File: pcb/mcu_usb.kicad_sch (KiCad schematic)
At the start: 31 parts, among them J12 USB_C_Receptacle, J13 UPDI, U10 CP2102N-A02-GQFN24, U11 LP2985-3.3, U9 AVR128DA32-I/PT, Y1 32.768kHz

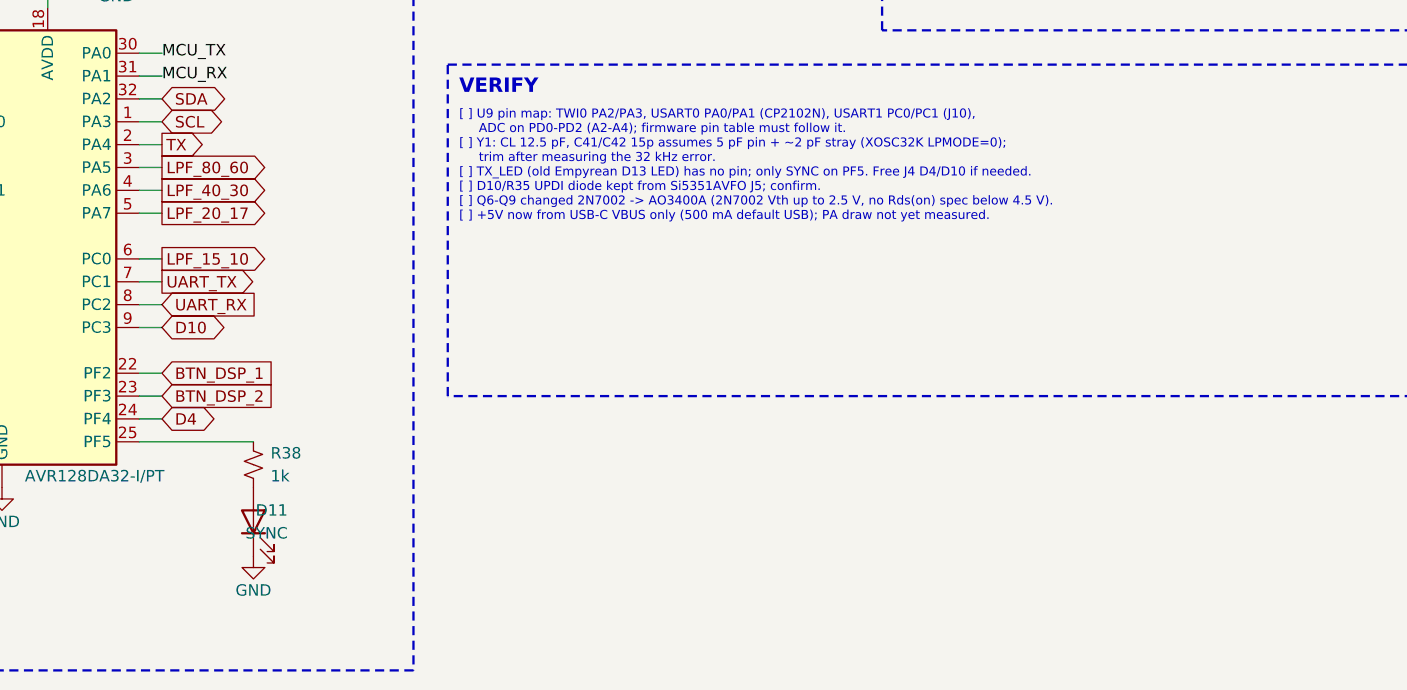
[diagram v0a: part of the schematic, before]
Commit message: Add TX LED on TX keying net; fix USART1 pin assignment
- D12 KT-0603YG (C2289) + R39 470R (C23179) from TX (PA4) to GND, ~2.6 mA
- PC0/PC1 now UART_TX/UART_RX (USART1 default pins), LPF_15_10 moved to PC2
- ERC 0 errors; PDF regenerated; VERIFY.md TX_LED item resolved
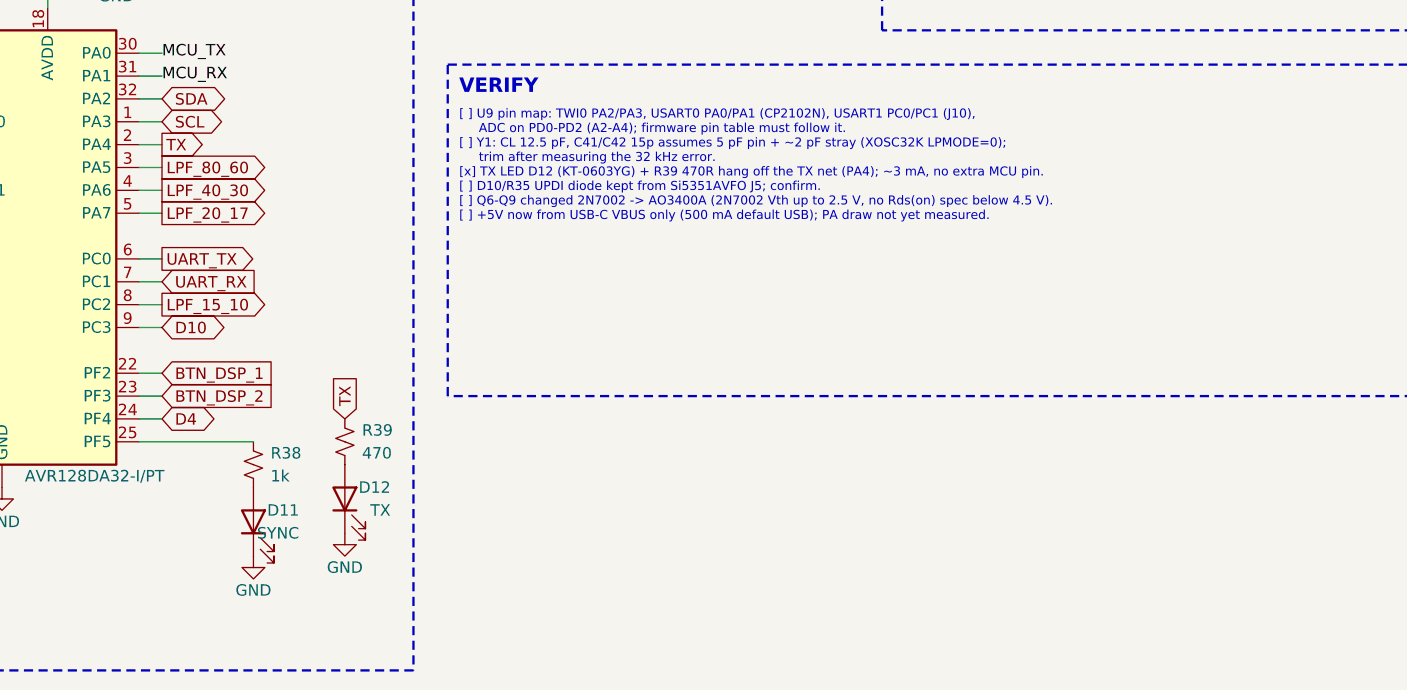
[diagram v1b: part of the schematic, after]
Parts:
- added D12: TX, LED_SMD:LED_0603_1608Metric, symbol Device:LED
- added R39: 470, Resistor_SMD:R_0603_1608Metric, symbol Device:R_Small_US
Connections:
- net GND: now also D12.1 (K)
- net LPF_15_10: now also U9.8 (PC2); no longer U9.6 (PC0)
- net TX: now also R39.1
- net UART_RX: now also U9.7 (PC1); no longer U9.8 (PC2)
- net UART_TX: now also U9.6 (PC0); no longer U9.7 (PC1)
- new net: D12.2 (A), R39.2
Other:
- note added: "[ ] U9 pin map: TWI0 PA2/PA3, USART0 PA0/PA1 (CP2102N), USART1 PC0/PC1 (J10), ADC on PD0-PD2 (A2-A4); firmware pin table must follow it. [ ] Y1: CL 12.5 pF, C41/C42 15p assumes 5 pF pin + ~2 pF stray (XOSC32K LPMODE=0); trim after measuring the 32 kHz error. [x] TX LED D12 (KT-0603YG) + R39 470R hang off the TX net (PA4); ~3 mA, no extra MCU pin. [ ] D10/R35 UPDI diode kept from Si5351AVFO J5; co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"
- note removed: "[ ] U9 pin map: TWI0 PA2/PA3, USART0 PA0/PA1 (CP2102N), USART1 PC0/PC1 (J10), ADC on PD0-PD2 (A2-A4); firmware pin table must follow it. [ ] Y1: CL 12.5 pF, C41/C42 15p assumes 5 pF pin + ~2 pF stray (XOSC32K LPMODE=0); trim after measuring the 32 kHz error. [ ] TX_LED (old Empyrean D13 LED) has no pin; only SYNC on PF5. Free J4 D4/D10 if needed. [ ] D10/R35 UPDI diode kept from Si5351AVFO J5; co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"

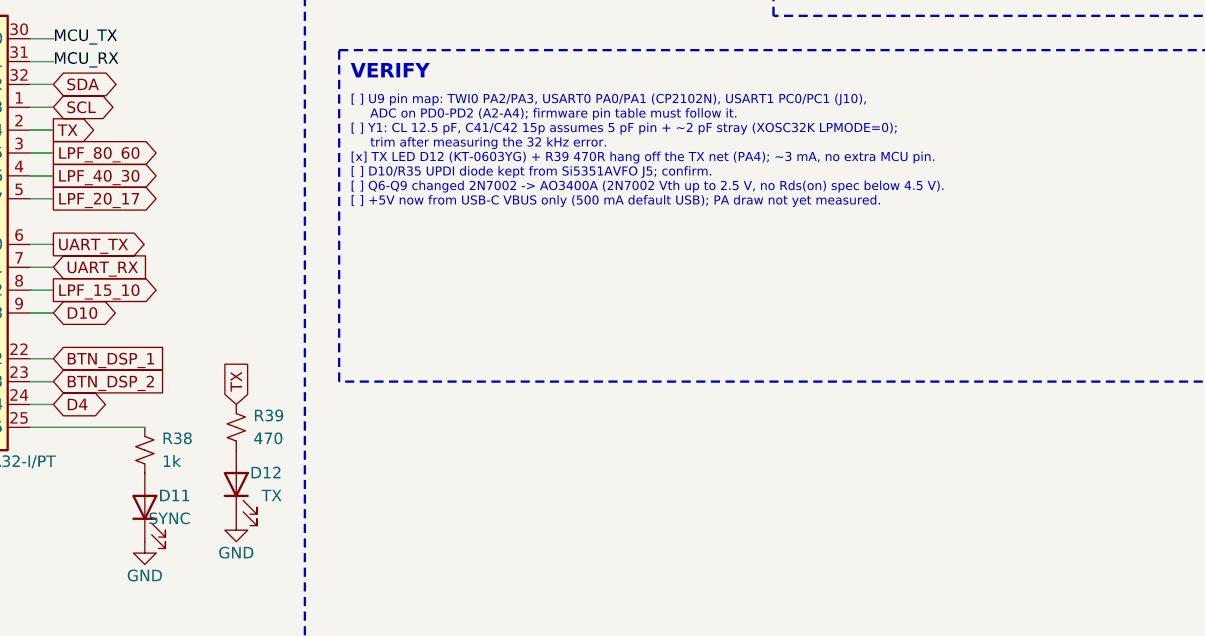
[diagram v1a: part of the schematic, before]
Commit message: Sync LED to yellow KT-0603Y with 470R; confirm UPDI matches Si5351AVFO/EtherKeyerMini
- D11 KT-0603Y (C2287), R38 470R (C23179), ~2-3 mA
- VERIFY.md: UPDI and sync LED items resolved; U1 FB stays open
- ERC 0 errors; PDF regenerated
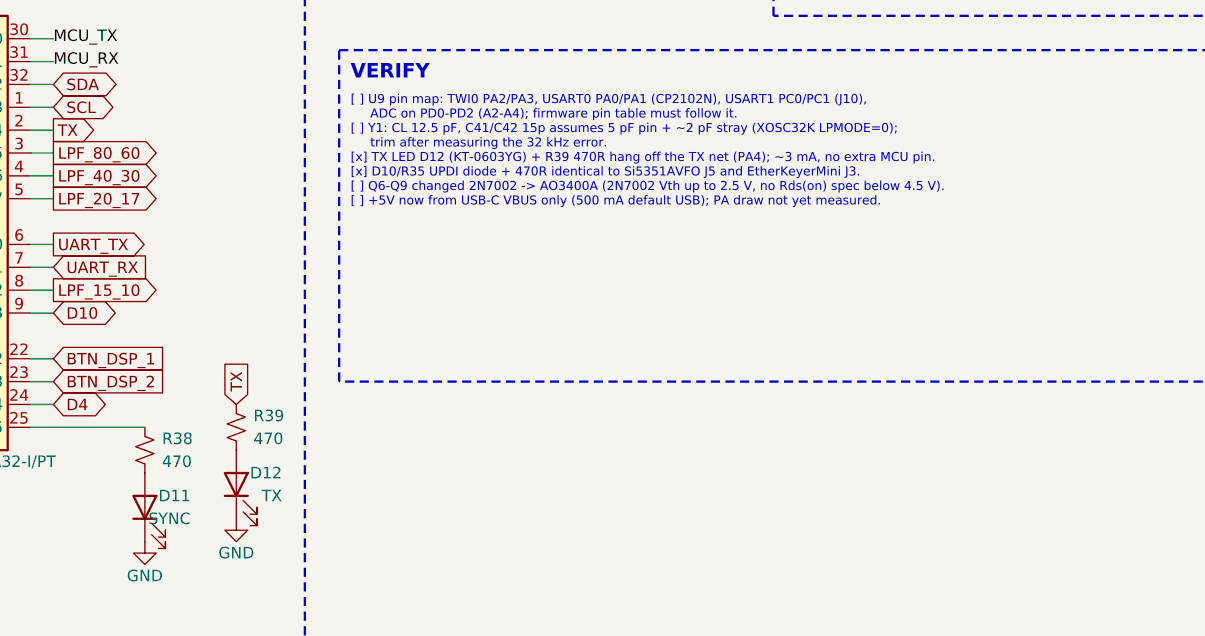
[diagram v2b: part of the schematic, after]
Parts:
- D11: LCSC C2286 -> C2287; MPN KT-0603R -> KT-0603Y
- R38: value 1k -> 470; LCSC C21190 -> C23179; MPN 0603WAF1001T5E -> 0603WAF4700T5E
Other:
- note added: "[ ] U9 pin map: TWI0 PA2/PA3, USART0 PA0/PA1 (CP2102N), USART1 PC0/PC1 (J10), ADC on PD0-PD2 (A2-A4); firmware pin table must follow it. [ ] Y1: CL 12.5 pF, C41/C42 15p assumes 5 pF pin + ~2 pF stray (XOSC32K LPMODE=0); trim after measuring the 32 kHz error. [x] TX LED D12 (KT-0603YG) + R39 470R hang off the TX net (PA4); ~3 mA, no extra MCU pin. [x] D10/R35 UPDI diode + 470R identical to Si5351A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"
- note removed: "[ ] U9 pin map: TWI0 PA2/PA3, USART0 PA0/PA1 (CP2102N), USART1 PC0/PC1 (J10), ADC on PD0-PD2 (A2-A4); firmware pin table must follow it. [ ] Y1: CL 12.5 pF, C41/C42 15p assumes 5 pF pin + ~2 pF stray (XOSC32K LPMODE=0); trim after measuring the 32 kHz error. [x] TX LED D12 (KT-0603YG) + R39 470R hang off the TX net (PA4); ~3 mA, no extra MCU pin. [ ] D10/R35 UPDI diode kept from Si5351AVFO J5; co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"
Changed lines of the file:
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@@
 			)
 		)
-		(property "Value" "1k"
+		(property "Value" "470"
 			(at 131.445 173.99 0)
 			(effects
@@
 			)
 		)
-		(property "MPN" "0603WAF1001T5E"
+		(property "MPN" "0603WAF4700T5E"
 			(at 129.54 172.72 0)
 			(effects
@@
 			)
 		)
-		(property "LCSC" "C21190"
+		(property "LCSC" "C23179"
 			(at 129.54 172.72 0)
 			(effects
@@
 			)
 		)
-		(property "MPN" "KT-0603R"
+		(property "MPN" "KT-0603Y"
 			(at 129.54 179.07 0)
 			(effects
@@
 			)
 		)
-		(property "LCSC" "C2286"
+		(property "LCSC" "C2287"
 			(at 129.54 179.07 0)
 			(effects
@@
 		)
 	)
-	(text "[ ] U9 pin map: TWI0 PA2/PA3, USART0 PA0/PA1 (CP2102N), USART1 PC0/PC1 (J10),\n     ADC on PD0-PD2 (A2-A4); firmware pin table must follow it.\n[ ] Y1: CL 12.5 pF, C41/C42 15p assumes 5 pF pin + ~2 pF stray (XOSC32K LPMODE=0);\n     trim after measuring the 32 kHz error.\n[x] TX LED D12 (KT-0603YG) + R39 470R hang off the TX net (PA4); ~3 mA, no extra MCU pin.\n[ ] D10/R35 UPDI diode kept from Si5351AVFO J5; confirm.\n[ ] Q6-Q9 changed 2N7002 -> AO3400A (2N7002 Vth up to 2.5 V, no Rds(on) spec below 4.5 V).\n[ ] +5V now from USB-C VBUS only (500 mA default USB); PA draw not yet measured."
+	(text "[ ] U9 pin map: TWI0 PA2/PA3, USART0 PA0/PA1 (CP2102N), USART1 PC0/PC1 (J10),\n     ADC on PD0-PD2 (A2-A4); firmware pin table must follow it.\n[ ] Y1: CL 12.5 pF, C41/C42 15p assumes 5 pF pin + ~2 pF stray (XOSC32K LPMODE=0);\n     trim after measuring the 32 kHz error.\n[x] TX LED D12 (KT-0603YG) + R39 470R hang off the TX net (PA4); ~3 mA, no extra MCU pin.\n[x] D10/R35 UPDI diode + 470R identical to Si5351AVFO J5 and EtherKeyerMini J3.\n[ ] Q6-Q9 changed 2N7002 -> AO3400A (2N7002 Vth up to 2.5 V, no Rds(on) spec below 4.5 V).\n[ ] +5V now from USB-C VBUS only (500 mA default USB); PA draw not yet measured."
 		(exclude_from_sim no)
 		(at 152.4 133.35 0)

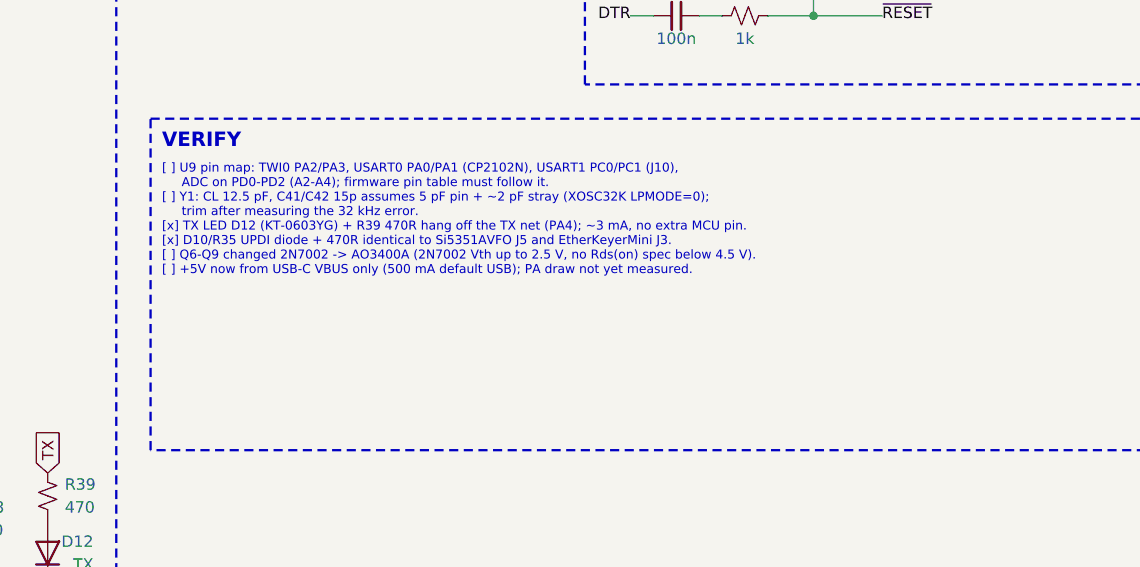
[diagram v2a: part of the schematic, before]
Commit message: VERIFY: resolve U1 FB item (FB tied to VIN selects internal 12 V output)
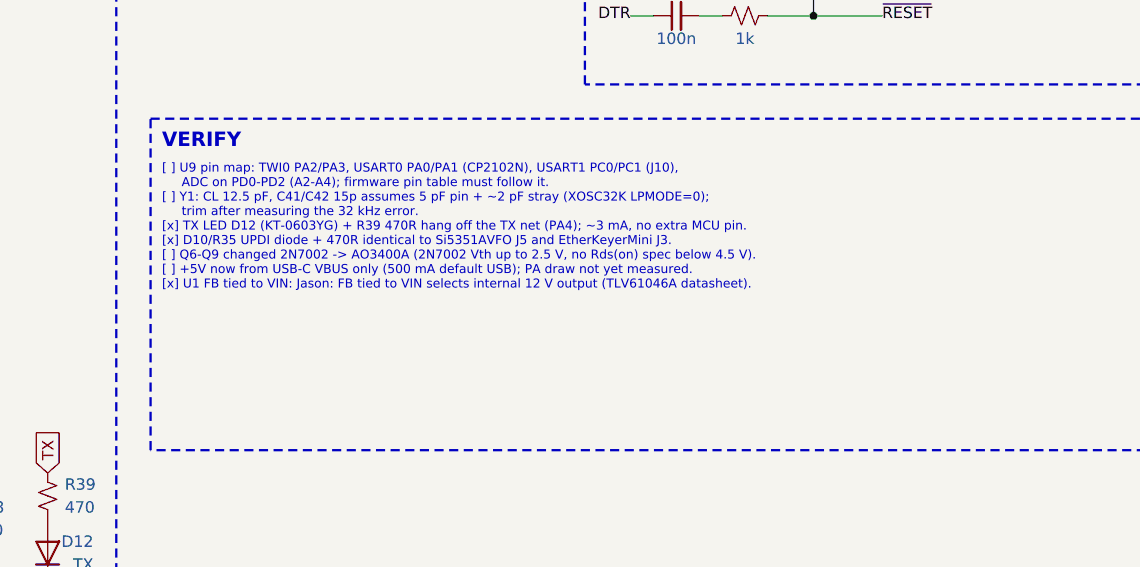
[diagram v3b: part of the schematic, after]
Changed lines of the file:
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@@
 		)
 	)
-	(text "[ ] U9 pin map: TWI0 PA2/PA3, USART0 PA0/PA1 (CP2102N), USART1 PC0/PC1 (J10),\n     ADC on PD0-PD2 (A2-A4); firmware pin table must follow it.\n[ ] Y1: CL 12.5 pF, C41/C42 15p assumes 5 pF pin + ~2 pF stray (XOSC32K LPMODE=0);\n     trim after measuring the 32 kHz error.\n[x] TX LED D12 (KT-0603YG) + R39 470R hang off the TX net (PA4); ~3 mA, no extra MCU pin.\n[x] D10/R35 UPDI diode + 470R identical to Si5351AVFO J5 and EtherKeyerMini J3.\n[ ] Q6-Q9 changed 2N7002 -> AO3400A (2N7002 Vth up to 2.5 V, no Rds(on) spec below 4.5 V).\n[ ] +5V now from USB-C VBUS only (500 mA default USB); PA draw not yet measured."
+	(text "[ ] U9 pin map: TWI0 PA2/PA3, USART0 PA0/PA1 (CP2102N), USART1 PC0/PC1 (J10),\n     ADC on PD0-PD2 (A2-A4); firmware pin table must follow it.\n[ ] Y1: CL 12.5 pF, C41/C42 15p assumes 5 pF pin + ~2 pF stray (XOSC32K LPMODE=0);\n     trim after measuring the 32 kHz error.\n[x] TX LED D12 (KT-0603YG) + R39 470R hang off the TX net (PA4); ~3 mA, no extra MCU pin.\n[x] D10/R35 UPDI diode + 470R identical to Si5351AVFO J5 and EtherKeyerMini J3.\n[ ] Q6-Q9 changed 2N7002 -> AO3400A (2N7002 Vth up to 2.5 V, no Rds(on) spec below 4.5 V).\n[ ] +5V now from USB-C VBUS only (500 mA default USB); PA draw not yet measured.\n[x] U1 FB tied to VIN: Jason: FB tied to VIN selects internal 12 V output (TLV61046A datasheet)."
 		(exclude_from_sim no)
 		(at 152.4 133.35 0)
